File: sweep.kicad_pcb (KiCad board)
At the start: 2 copper layers, 216.9 x 86.9 mm, 221 parts, among them J1 USB_C_Receptacle_USB2.0_16P, J11 Conn_01x01, J12 Conn_01x01, J13 Conn_01x01, J2 Conn_01x01, J3 USB_C_Receptacle_USB2.0_16P, J4 USB_C_Receptacle_USB2.0_16P, J5 USB_C_Receptacle_USB2.0_16P, J6 Conn_01x08, J7 Conn_01x08, SW1 SW_Push, SW10 SW_Push, SW11 SW_Push, SW12 SW_Push, SW13 SW_Push, SW14 SW_Push, SW15 SW_Push, SW16 SW_Push, SW17 SW_Push, SW18 SW_Push, SW19 SW_Push, SW2 SW_Push, SW20 SW_Push, SW21 SW_Push, SW22 SW_Push, SW23 SW_Push, SW24 SW_Push, SW25 SW_Push, SW26 SW_Push, SW27 SW_Push, SW28 SW_Push, SW29 SW_Push, SW3 SW_Push, SW30 SW_Push, SW31 SW_Push, SW32 SW_Push, SW33 SW_Push, SW34 SW_Push, SW35 SW_Push, SW36 SW_Push, SW37 SW_Push, SW38 SW_Push, SW4 SW_Push, SW5 SW_Push, SW6 SW_Push, SW7 SW_Push, SW8 SW_Push, SW9 SW_Push, U1 RP2040, U10 SN74LVC1T45DRL, U11 INA138, U12 INA138, U2 XC6206PxxxMR, U3 SRV05-4, U4 W25Q128JVS, U5 RP2040, U6 SRV05-4, U7 XC6206PxxxMR, U8 W25Q128JVS, U9 SN74LVC1T45DRL, Y1 Crystal_GND24, Y2 Crystal_GND24

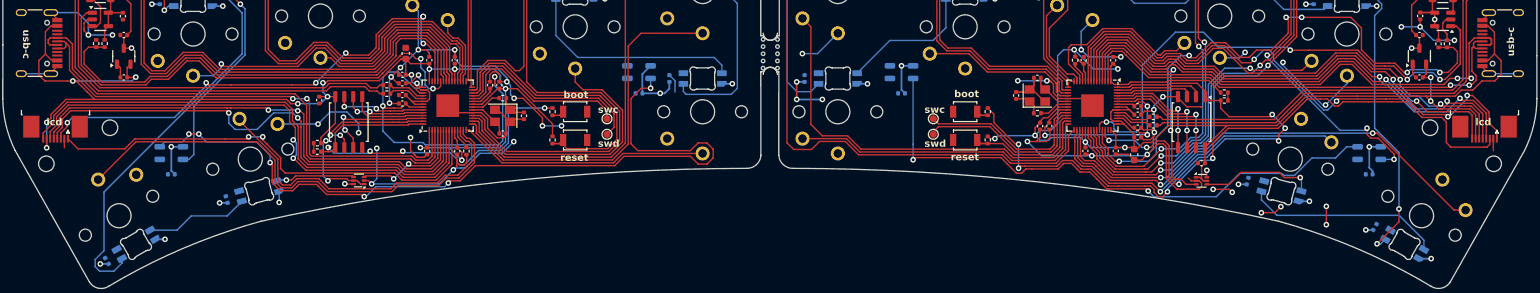
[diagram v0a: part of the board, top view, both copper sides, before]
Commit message: Fix FPC connector pinout, minor readme syntax updates
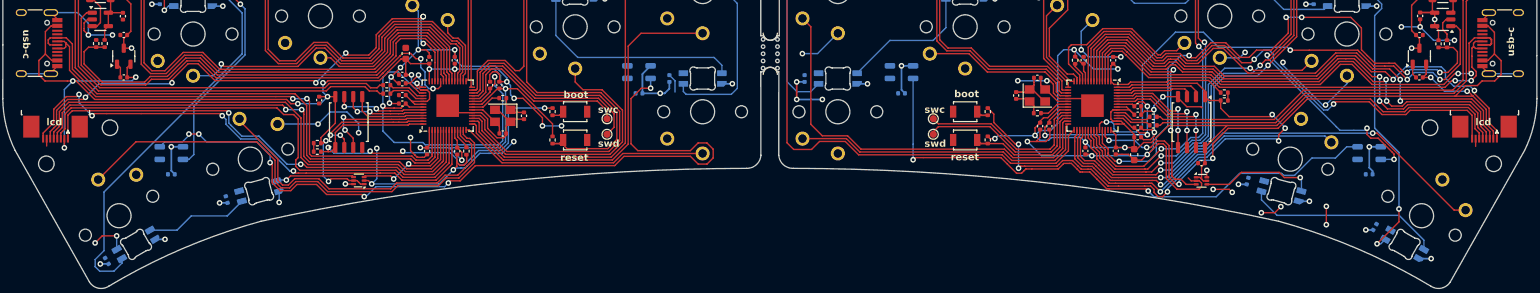
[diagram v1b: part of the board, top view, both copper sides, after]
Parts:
- removed J7: Conn_01x08, Connector_FFC-FPC:TE_0-1734839-8_1x08-1MP_P0.5mm_Horizontal
- added J8: Conn_01x08_MountingPin, Connector_FFC-FPC:TE_0-1734839-8_1x08-1MP_P0.5mm_Horizontal, F.Cu at (251.5, 115.2)
- J6: value Conn_01x08 -> Conn_01x08_MountingPin
- moved J6 202.1 mm to (49.5, 115.2)
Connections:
- J6 pad 1: LCD_BL_L -> LCD_CS_R
- J6 pad 2: GND -> +3V3
- J6 pad 3: LCD_RST_L -> SPI_SCK_R
- J6 pad 4: SPI_MISO_L -> SPI_MOSI_R
- J6 pad 5: SPI_MOSI_L -> SPI_MISO_R
- J6 pad 6: SPI_SCK_L -> LCD_RST_R
- J6 pad 7: +3V3 -> GND
- J6 pad 8: LCD_CS_L -> LCD_BL_R
- J6 pad MP: (no net) -> GND
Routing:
- net LCD_BL_R: track 65.1 -> 74.1 mm, vias 2 -> 4
- net LCD_CS_R: track 73.3 -> 66.9 mm, vias 0 -> 2
- net LCD_BL_L: track 79.6 -> 73.9 mm, vias 4 -> 2
- net LCD_CS_L: track 69.7 -> 75.2 mm
- net +5V: track 115.7 -> 121.0 mm, vias 39 -> 41
- net LCD_RST_R: track 71.3 -> 75.8 mm
- net LCD_RST_L: track 73.9 -> 70.9 mm
- net SPI_SCK_L: track 73.9 -> 76.4 mm
- net SPI_SCK_R: track 73.7 -> 72.4 mm, vias 2 -> 0
- net SPI_MOSI_L: track 70.9 -> 72.1 mm
- net GND: track 461.1 -> 460.2 mm
- net SPI_MOSI_R: track 69.5 -> 70.2 mm
- net SPI_MISO_R: track 71.8 -> 71.4 mm, vias 2 -> 0
- net +3V3: track 395.7 -> 395.6 mm, vias 24 -> 23

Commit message: Update silkscreen graphics, BOM, and gerbers
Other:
- board text added: "commit: 0f7cde2 git.pngu.org/sweep"
- board text removed: "commit: f1ab047 git.pngu.org/sweep"
